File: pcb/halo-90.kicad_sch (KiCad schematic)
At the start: 102 parts, among them J1 TC2030-SWIM-NL, U1 STM8151G6U6, U2 SC7A20HTR, U3 DRV5032

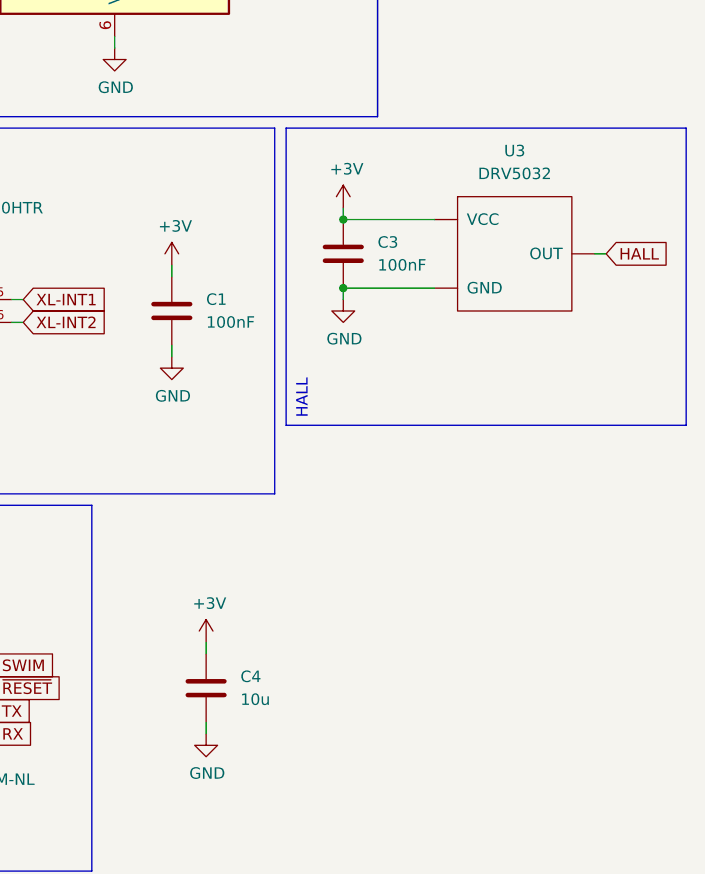
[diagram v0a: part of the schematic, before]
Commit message: fix(pcb): final component property fixes for JLCPCB
- U3 swapped to HAL2041SO (C22400320)
- BT1 reverted to BAT-HLD-001 (C7501066)
- Forced JLCPCB identical parts grouping on C1/C2/C3 and R1/R2/R3
- Updated gerbers.zip
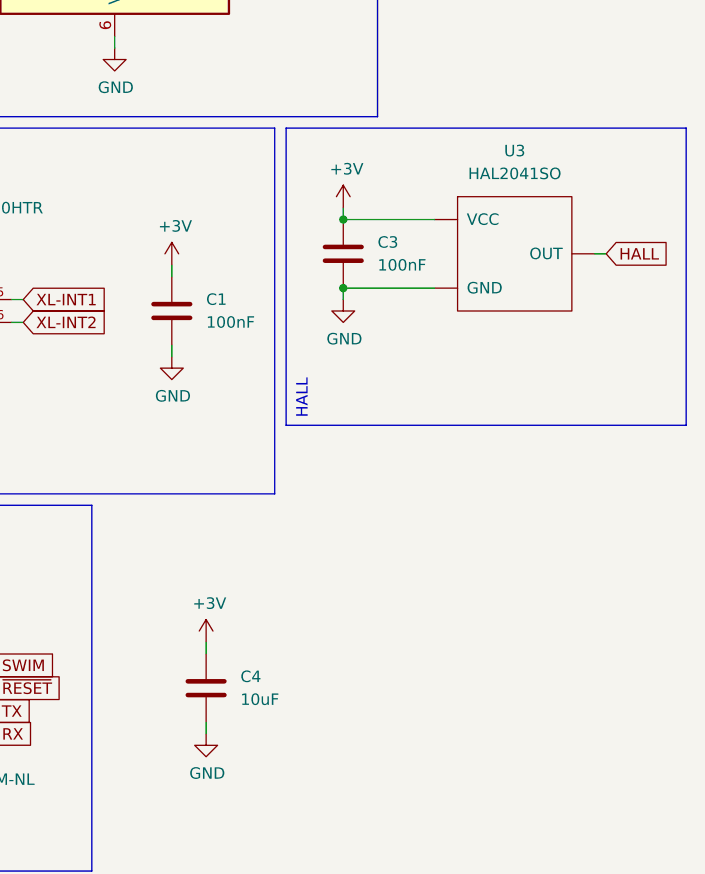
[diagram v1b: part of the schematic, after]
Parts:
- C4: value 10u -> 10uF
- U3: value DRV5032 -> HAL2041SO; LCSC Part# C130005 -> C22400320
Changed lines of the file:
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@@
 			)
 		)
-		(property "Value" "10u"
+		(property "Value" "10uF"
 			(at 227.33 156.2099 0)
 			(effects
@@
 			)
 		)
-		(property "Value" "DRV5032"
+		(property "Value" "HAL2041SO"
 			(at 257.81 97.79 0)
 			(effects
@@
 			)
 		)
-		(property "LCSC Part#" "C130005"
+		(property "LCSC Part#" "C22400320"
 			(at 257.81 123.19 0)
 			(effects

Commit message: chore(pcb): cleanup components and final manufacturing package regeneration
- Merged manual user footprint updates for SC7A20H, TC2030, tooling holes, and battery
- Regenerated strictly-grouped JLCPCB BOM
- Corrected CPL metric scale
- Removed old/unused component library files
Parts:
- removed U3: HAL2041SO, DRV5032:DRV5032, symbol DRV5032:DRV5032
- added R4: 10k, R-0402:R-0402, symbol R-0402:10k
- added U3: HAL2041SO, HAL2041SO:HAL2041SO, symbol HAL2041SO:HAL2041SO
- C1, C2, C3: LCSC Part # C85325 -> C1525
- C4: LCSC Part # C85325 -> C15525
- D1, D10, D11, D12, D13, D14, D15, D16, D17, D18, D19, D2, D20, D21, D22, D23, D24, D25, D26, D27, D28, D29, D3, D30, D31, D32, D33, D34, D35, D36, D37, D38, D39, D4, D40, D41, D42, D43, D44, D45, D46, D47, D48, D49, D5, D50, D51, D52, D53, D54, D55, D56, D57, D58, D59, D6, D60, D61, D62, D63, D64, D65, D66, D67, D68, D69, D7, D70, D71, D72, D73, D74, D75, D76, D77, D78, D79, D8, D80, D81, D82, D83, D84, D85, D86, D87, D88, D89, D9, D90: footprint BL-HUB37A-AV-TRB:D-0402 -> XL-1005SURC:XL-1005SURC; symbol BL-HUB37A-AV-TRB:BL-HUB37A-AV-TRB -> XL-1005SURC:XL-1005SURC; LCSC Part# (none) -> C25503345; MPN (none) -> XL-1005SURC; Manufacturer (none) -> XINGLIGHT
- J1: footprint TC2030-IDC-NL:Tag-Connect_TC2030-IDC-NL_2x03_P1.27mm_Vertical -> TC2030-IDC-NL:TC2030-IDC-NL
- R1, R3: LCSC Part # C85325 -> C25744
- U1: MPN (none) -> STM8151G6U6; Manufacturer (none) -> STMicroelectronics
- U2: LCSC Part# (none) -> C19274408; MPN (none) -> SC7A20HTR; Manufacturer (none) -> Hangzhou Silan Microelectronics
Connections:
- net +3V: now also R4.2, U3.1 (VCC)
- net GND: now also U3.3 (GND)
- net HALL: now also R4.1, U3.2 (OUT)
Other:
- moved on the sheet: C3

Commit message: fix(pcb): final LCSC property corrections for BOM generation
- Fixed user manual library edits that assigned the STM8 LCSC to the battery holder and removed it from the MCU
- Regenerated native BOM directly from updated KiCad component properties
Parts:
- BT1: LCSC Part # C85325 -> C7501066
- D1, D10, D11, D12, D13, D14, D15, D16, D17, D18, D19, D2, D20, D21, D22, D23, D24, D25, D26, D27, D28, D29, D3, D30, D31, D32, D33, D34, D35, D36, D37, D38, D39, D4, D40, D41, D42, D43, D44, D45, D46, D47, D48, D49, D5, D50, D51, D52, D53, D54, D55, D56, D57, D58, D59, D6, D60, D61, D62, D63, D64, D65, D66, D67, D68, D69, D7, D70, D71, D72, D73, D74, D75, D76, D77, D78, D79, D8, D80, D81, D82, D83, D84, D85, D86, D87, D88, D89, D9, D90: LCSC Part # (none) -> C25503345; LCSC Part# C25503345 -> (none)
- U1: LCSC Part # (none) -> C85325
- U2: LCSC C19274408 -> (none); LCSC Part # C85325 -> C19274408; LCSC Part# C19274408 -> (none)
- U3: LCSC Part # (none) -> C22400320

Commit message: fix(pcb): update BT1 value to BAT-HLD-001 and strictly format JLCPCB/Neoden YY1 PnP CSVs
- Changed battery holder (BT1) Comment/Value from CR-2032 to MPN BAT-HLD-001
- Regenerated mm-scale Pick and Place data utilizing custom Neoden YY1 and JLC parsers
- Wiped old unneeded tracked python scripts
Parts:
- BT1: value CR-2032 -> BAT-HLD-001
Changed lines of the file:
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@@
 			)
 		)
-		(property "Value" "CR-2032"
+		(property "Value" "BAT-HLD-001"
 			(at 246.7611 26.5493 90)
 			(effects

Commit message: Added CS trace and updated battery.
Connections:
- net +3V: now also U2.10 (CS)
- no-connect marks 9 -> 8
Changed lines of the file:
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@@
 	)
 	(no_connect
-		(at 184.15 116.84)
-	)
-	(no_connect
 		(at 198.12 71.12)
 	)
@@
 		)
 	)
+	(wire
+		(pts
+			(xy 182.88 116.84) (xy 184.15 116.84)
+		)
+		(stroke
+			(width 0)
+			(type default)
+		)
+	)
 	(polyline
 		(pts
@@
 	(wire
 		(pts
+			(xy 182.88 118.11) (xy 182.88 116.84)
+		)
+		(stroke
+			(width 0)
+			(type default)
+		)
+	)
+	(wire
+		(pts
 			(xy 120.65 137.16) (xy 116.84 137.16)
 		)
@@
 		)
 		(property "Value" "BAT-HLD-001"
-			(at 246.7611 26.5493 90)
+			(at 246.38 31.75 90)
 			(effects
 				(font
@@
 			)
 		)
-		(property "LCSC Part #" "C85325"
-			(effects (hide yes))
-		)
 		(property "Footprint" "STM8151G6U6:UFQFPN28"
 			(at 213.36 92.71 0)
@@
 			)
 		)
+		(property "LCSC Part #" "C85325"
+			(at -0.0001 -0.0001 0)
+			(effects
+				(font
+					(size 1.27 1.27)
+				)
+				(hide yes)
+			)
+		)
 		(property "Manufacturer" "STMicroelectronics"
 			(at 213.36 40.64 0)
@@
 					(unit 1)
 				)
+			)
+		)
+	)
+	(symbol
+		(lib_id "nets:+3V")
+		(at 182.88 118.11 180)
+		(unit 1)
+		(exclude_from_sim no)
+		(in_bom yes)
+		(on_board yes)
+		(dnp no)
+		(property "Reference" "#PWR012"
+			(at 182.88 114.3 0)
+			(effects
+				(font
+					(size 1.27 1.27)
+				)
+				(hide yes)
+			)
+		)
+		(property "Value" "+3V"
+			(at 182.5117 122.4344 0)
+			(effects
+				(font
+					(size 1.27 1.27)
+				)
+			)
+		)
+		(property "Footprint" ""
+			(at 182.88 118.11 0)
+			(effects
+				(font
+					(size 1.27 1.27)
+				)
+				(hide yes)
+			)
+		)
+		(property "Datasheet" ""
+			(at 182.88 118.11 0)
+			(effects
+				(font
+					(size 1.27 1.27)
+				)
+				(hide yes)
+			)
+		)
+		(property "Description" ""
+			(at 182.88 118.11 0)
+			(effects
+				(font
+					(size 1.27 1.27)
+				)
+			)
+		)
+		(pin "1"
+		)
+		(instances
+			(project "halo-90"
+				(path "/5b10fd11-3eea-4ed1-85e0-64e6a45ea671"
+					(reference "#PWR012")
+					(unit 1)
+				)

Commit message: Added mic and rerouted
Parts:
- added C5: 100nF, C-0402:C-0402, symbol C-0402:100n
- added Q1: ALS-PT19, ALS-PT19:ALS-PT19, symbol ALS-PT19:ALS Light
- added Q2: SPH0641LU4H, SPH0641LU4H:SPH0641LU4H, symbol SPH0641LU4H:SPH0641LU4H
- added R5: 10k, R-0402:R-0402, symbol R-0402:10k
- added TP1, TP2: TestPoint_D1.0, tooling:TestPoint_Pad_D1.0mm, symbol tooling:TestPoint_D1.0
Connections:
- net +3V: no longer C3.1, R4.2, U3.1 (VCC)
- net CPX-0: now also U1.14 (PB2); no longer U1.2 (PA2)
- net CPX-1: now also U1.10 (PD2); no longer U1.3 (PA3)
- net CPX-2: now also U1.9 (PD1); no longer U1.15 (PB3)
- net CPX-3: now also U1.8 (PD0); no longer U1.5 (PA5)
- net CPX-4: now also U1.17 (PB5); no longer U1.11 (PD3)
- net CPX-5: now also U1.13 (PB1); no longer U1.10 (PD2)
- net CPX-6: now also U1.12 (PB0); no longer U1.9 (PD1)
- net CPX-7: now also U1.16 (PB4); no longer U1.4 (PA4)
- net CPX-8: now also U1.11 (PD3); no longer U1.18 (PB6)
- net CPX-9: now also U1.15 (PB3); no longer U1.17 (PB5)
- net GND: now also U2.1 (SDO), C5.2, Q2.2 (SELECT), Q2.3 (GROUND), R5.1
- net HALL: now also U1.2 (PA2); no longer U1.8 (PD0)
- net RX: now also J1.2 (TX); no longer J1.1 (RX)
- net TX: now also J1.1 (RX); no longer J1.2 (TX)
- net XL-INT1: no longer U1.20 (PD4)
- net XL-INT2: no longer U1.19 (PB7)
- new net ALR: Q1.2 (Emitter), R5.2, U1.5 (PA5)
- new net ALR_{PWR}: Q1.1 (Collector), U1.4 (PA4)
- new net HALL_{PWR}: C3.1, R4.2, U1.3 (PA3), U3.1 (VCC)
- new net PDM_CLK: Q2.4 (CLOCK), TP2.1, U1.19 (PB7)
- new net PDM_DTA: Q2.1 (DATA), TP1.1, U1.18 (PB6)
- new net PWR_{MIC}: C5.1, Q2.5 (V_{DD}), U1.20 (PD4)
- no-connect marks 8 -> 3

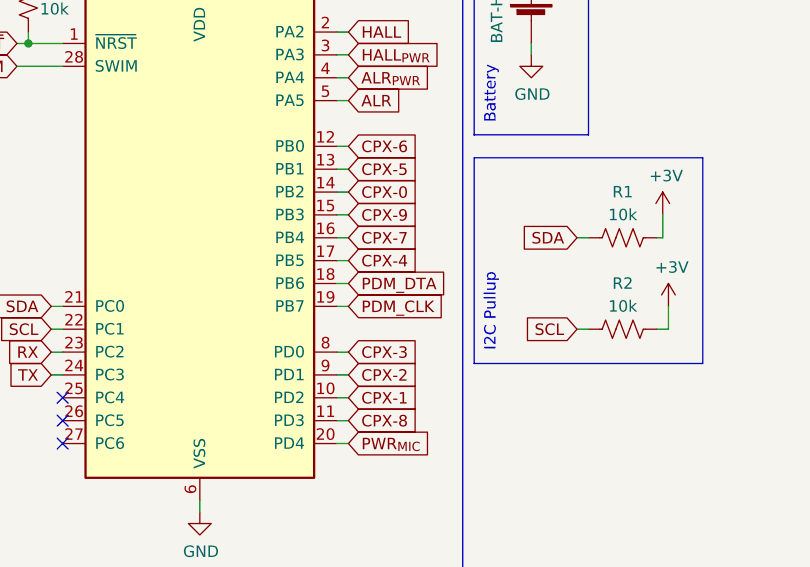
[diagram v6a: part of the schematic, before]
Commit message: 0v9 with ALR, XL, Mic added order placed
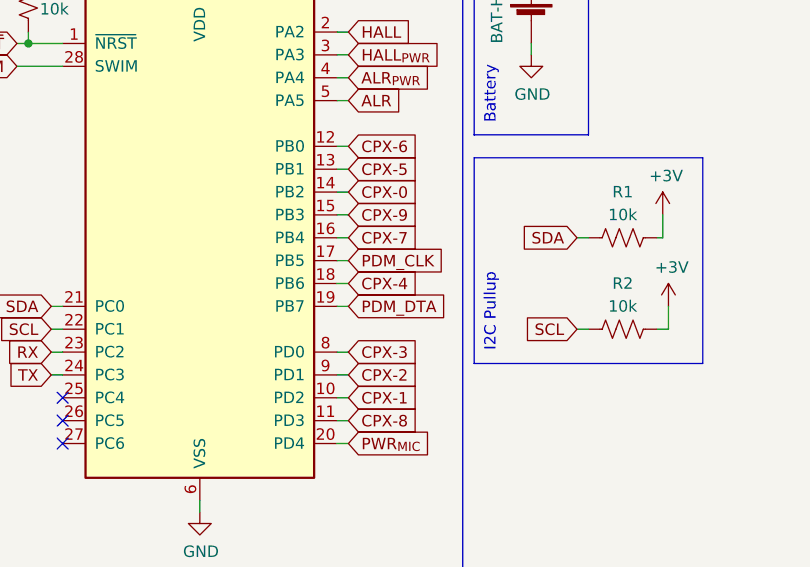
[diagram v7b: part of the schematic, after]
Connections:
- net CPX-4: now also U1.18 (PB6); no longer U1.17 (PB5)
- net PDM_CLK: now also U1.17 (PB5); no longer U1.19 (PB7)
- net PDM_DTA: now also U1.19 (PB7); no longer U1.18 (PB6)
